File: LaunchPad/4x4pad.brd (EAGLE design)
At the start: 127 x 102.5 mm, 17 parts

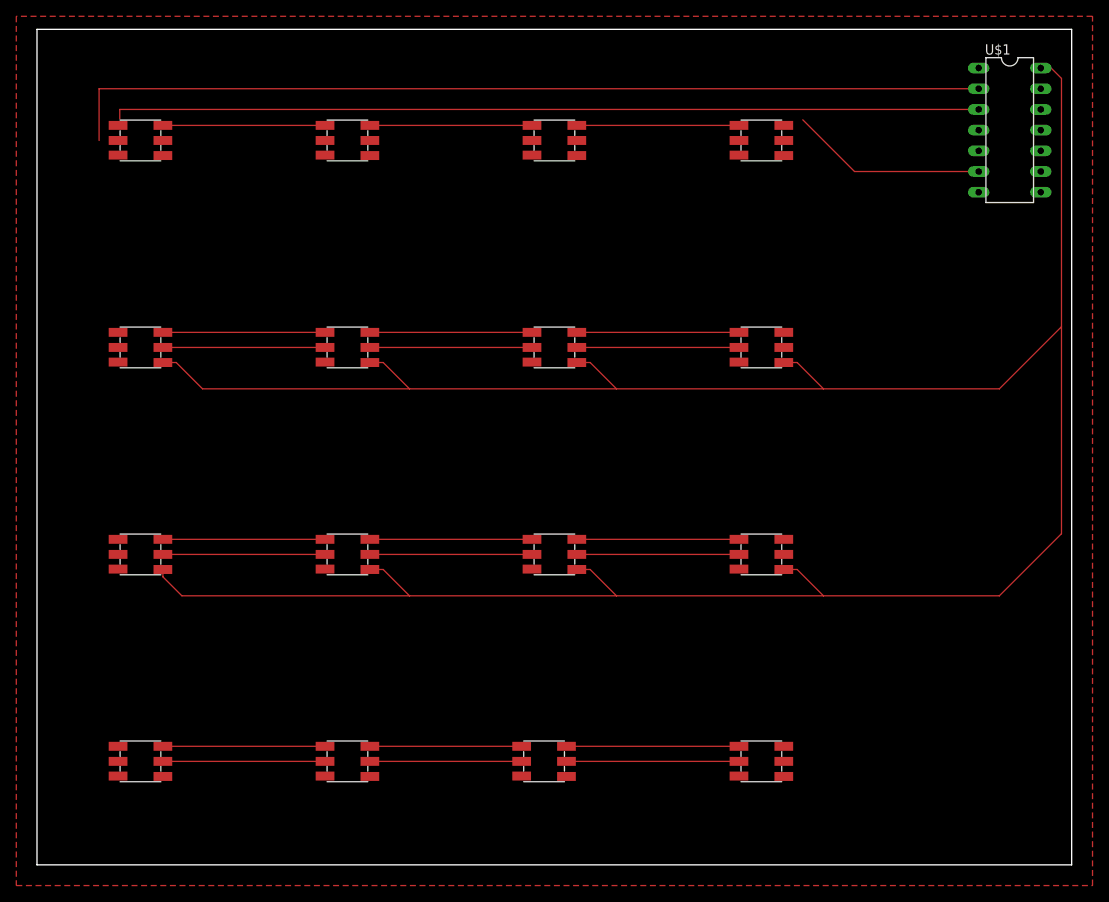
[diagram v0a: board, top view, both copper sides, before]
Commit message: Restarted 4x4 board, still need vertical button jumpoers, button connection
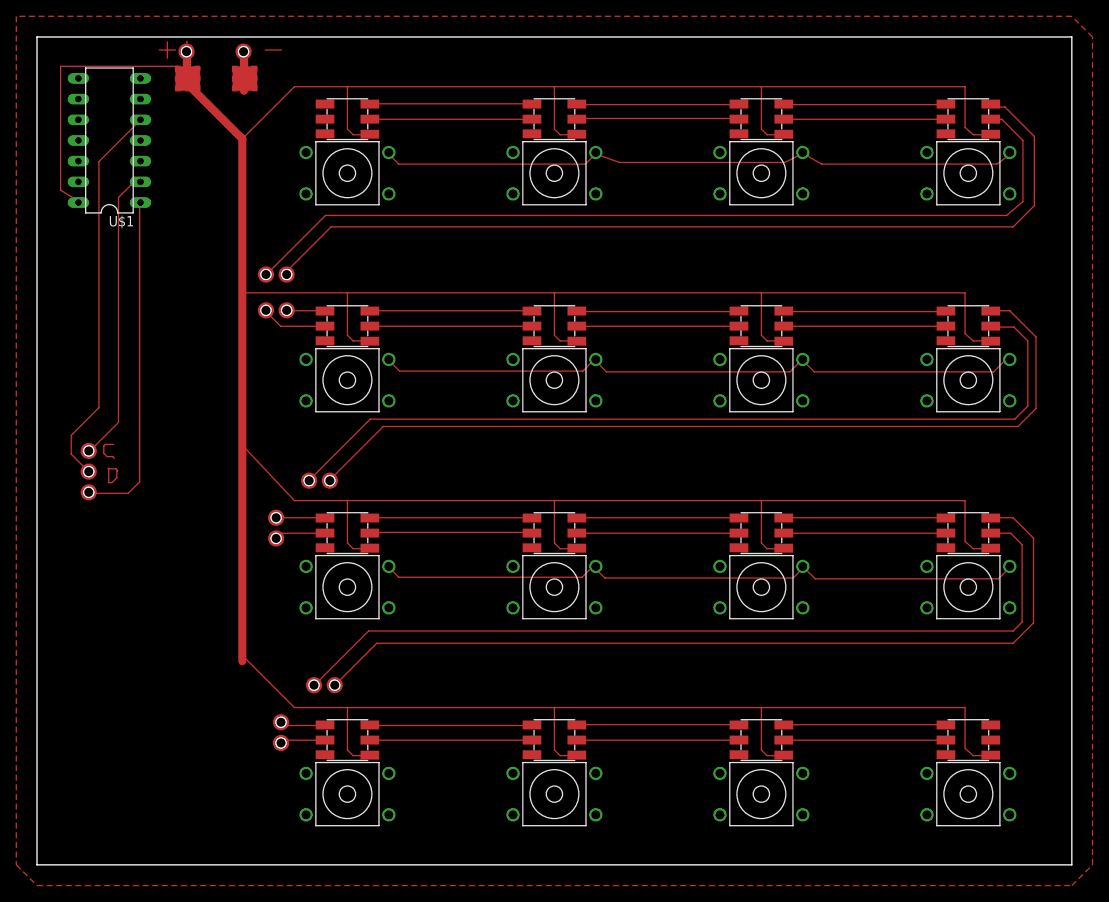
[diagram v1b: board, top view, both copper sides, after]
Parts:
- added U$18, U$19, U$20, U$21, U$22, U$23, U$24, U$25, U$26, U$27, U$28, U$29, U$30, U$31, U$32, U$33: SOFT-TACTILE-PUSHBUTTON, launchpadParts:ADAFRUIT-SOFT-TACTILE-PUSHBUTTON
- moved U$1 110.5 mm to (8.89, 88.9), turned to 90 degrees
- moved U$16 26.8 mm to (88.9, 15.3)
- moved U$12 25.5 mm to (88.9, 40.7)
- moved U$4 25.5 mm to (88.9, 91.5)
- moved U$8 25.5 mm to (88.9, 66.1)
- moved U$10 25.5 mm to (38.1, 40.7)
- moved U$14 25.5 mm to (38.1, 15.3)
- moved U$2 25.5 mm to (38.1, 91.5)
- moved U$6 25.5 mm to (38.1, 66.1)
- moved U$11 25.5 mm to (63.5, 40.7)
- moved U$15 25.5 mm to (63.5, 15.3)
- moved U$3 25.5 mm to (63.5, 91.5)
- moved U$7 25.5 mm to (63.5, 66.1)
- moved U$13 25.5 mm to (114.3, 40.7)
- moved U$17 25.5 mm to (114.3, 15.3)
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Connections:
- net +5V renamed N$36
- net GND renamed N$37
- new net COL1: U$18.P$1, U$18.P$2, U$30.P$1, U$30.P$2
- new net COL2: U$19.P$1, U$19.P$2, U$31.P$1, U$31.P$2
- new net COL3: U$20.P$1, U$20.P$2, U$32.P$1, U$32.P$2
- new net COL4: U$21.P$1, U$21.P$2, U$33.P$1, U$33.P$2
- new net ROW1: U$18.P$3, U$18.P$4, U$19.P$3, U$19.P$4, U$20.P$3, U$20.P$4, U$21.P$3, U$21.P$4
- new net ROW2: U$22.P$3, U$22.P$4, U$23.P$3, U$23.P$4, U$24.P$3, U$24.P$4, U$25.P$3, U$25.P$4
- new net ROW3: U$26.P$3, U$26.P$4, U$27.P$3, U$27.P$4, U$28.P$3, U$28.P$4, U$29.P$3, U$29.P$4
- new net ROW4: U$30.P$3, U$30.P$4, U$31.P$3, U$31.P$4, U$32.P$3, U$32.P$4, U$33.P$3, U$33.P$4
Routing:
- net N$36: track 326.3 -> 0.00 mm
- net N$31: track 0.00 -> 173.2 mm
- net CLK3.3: track 114.3 -> 0.00 mm
- net N$94: track 0.00 -> 110.6 mm
- net N$93: track 0.00 -> 108.5 mm
- net CLK5: track 106.6 -> 0.00 mm
- net N$102: track 0.00 -> 106.1 mm
- net N$105: track 0.00 -> 105.6 mm
- net N$103: track 0.00 -> 104.9 mm
- net N$104: track 0.00 -> 104.0 mm
- net N$40: track 0.00 -> 100.1 mm
- net N$86: track 0.00 -> 99.8 mm
- net N$56: track 0.00 -> 97.1 mm
- net N$97: track 0.00 -> 79.2 mm
- net N$96: track 0.00 -> 52.8 mm
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- added copper zone on layer 1, net GND
- added copper zone on layer 1, net VCC
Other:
- board size 127 x 102.5 mm -> 127 x 101.6 mm

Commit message: idk what I did
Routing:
- net N$118: track 0.00 -> 5.94 mm
- net N$116: track 0.00 -> 5.94 mm
- net N$114: track 0.00 -> 5.94 mm
- net N$113: track 0.00 -> 5.94 mm
- net N$120: track 0.00 -> 5.94 mm
- net N$115: track 0.00 -> 5.94 mm
- net N$112: track 0.00 -> 5.94 mm
- net N$119: track 0.00 -> 5.94 mm
- net N$117: track 0.00 -> 5.94 mm
- net N$92: track 0.00 -> 4.90 mm
- net N$110: track 0.00 -> 4.90 mm
- net N$109: track 0.00 -> 4.90 mm
- net N$107: track 0.00 -> 4.90 mm
- net N$111: track 0.00 -> 4.90 mm
- net N$108: track 0.00 -> 4.90 mm
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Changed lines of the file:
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@@
 <hole x="36.54" y="22.05" drill="1.27"/>
 <circle x="36.54" y="22.05" radius="0.803215625" width="0.381" layer="1"/>
+<hole x="104.3" y="82.35" drill="1.27"/>
+<circle x="104.3" y="82.35" radius="0.803215625" width="0.381" layer="1"/>
+<hole x="78.9" y="82.25" drill="1.27"/>
+<circle x="78.9" y="82.25" radius="0.803215625" width="0.381" layer="1"/>
+<hole x="53.5" y="82.25" drill="1.27"/>
+<circle x="53.5" y="82.25" radius="0.803215625" width="0.381" layer="1"/>
+<hole x="104.4" y="56.85" drill="1.27"/>
+<circle x="104.4" y="56.85" radius="0.803215625" width="0.381" layer="1"/>
+<hole x="78.9" y="56.85" drill="1.27"/>
+<circle x="78.9" y="56.85" radius="0.803215625" width="0.381" layer="1"/>
+<hole x="53.5" y="56.85" drill="1.27"/>
+<circle x="53.5" y="56.85" radius="0.803215625" width="0.381" layer="1"/>
+<hole x="53.5" y="31.45" drill="1.27"/>
+<circle x="53.5" y="31.45" radius="0.803215625" width="0.381" layer="1"/>
+<hole x="78.9" y="31.45" drill="1.27"/>
+<circle x="78.9" y="31.45" radius="0.803215625" width="0.381" layer="1"/>
+<hole x="104.3" y="31.45" drill="1.27"/>
+<circle x="104.3" y="31.45" radius="0.803215625" width="0.381" layer="1"/>
+<hole x="53.5" y="64.55" drill="1.27"/>
+<circle x="53.5" y="64.55" radius="0.803215625" width="0.381" layer="1"/>
+<hole x="79" y="64.55" drill="1.27"/>
+<circle x="79" y="64.55" radius="0.803215625" width="0.381" layer="1"/>
+<hole x="104.3" y="64.55" drill="1.27"/>
+<circle x="104.3" y="64.55" radius="0.803215625" width="0.381" layer="1"/>
+<hole x="53.6" y="39.15" drill="1.27"/>
+<circle x="53.6" y="39.15" radius="0.803215625" width="0.381" layer="1"/>
+<hole x="79" y="39.15" drill="1.27"/>
+<circle x="79" y="39.15" radius="0.803215625" width="0.381" layer="1"/>
+<hole x="104.4" y="39.25" drill="1.27"/>
+<circle x="104.4" y="39.25" radius="0.803215625" width="0.381" layer="1"/>
+<hole x="104.3" y="13.75" drill="1.27"/>
+<circle x="104.3" y="13.75" radius="0.803215625" width="0.381" layer="1"/>
+<hole x="78.9" y="13.75" drill="1.27"/>
+<circle x="78.9" y="13.75" radius="0.803215625" width="0.381" layer="1"/>
+<hole x="53.5" y="13.75" drill="1.27"/>
+<circle x="53.5" y="13.75" radius="0.803215625" width="0.381" layer="1"/>
 </plain>
 <attributes>
@@
 <wire x1="111.6" y1="91.5" x2="111.6" y2="91.4" width="0.1524" layer="1"/>
 </signal>
-<signal name="N$49">
-<wire x1="109.4" y1="31.3" x2="109.2" y2="31.3" width="0.1524" layer="1"/>
-</signal>
-<signal name="N$50">
-<wire x1="109.5" y1="57.1" x2="109.4" y2="57.1" width="0.1524" layer="1"/>
-</signal>
 <signal name="N$51">
 <wire x1="119.6" y1="87.3" x2="117.8" y2="86" width="0.1524" layer="1"/>
@@
 <wire x1="29.9" y1="66.1" x2="28.1" y2="67.9" width="0.125" layer="1"/>
 </signal>
+<signal name="N$92">
+<wire x1="104.3" y1="82.4" x2="109.2" y2="82.4" width="0.1524" layer="1"/>
+</signal>
+<signal name="N$106">
+<wire x1="78.9" y1="82.3" x2="83.8" y2="82.3" width="0.1524" layer="1"/>
+</signal>
+<signal name="N$107">
+<wire x1="53.5" y1="82.3" x2="58.4" y2="82.3" width="0.1524" layer="1"/>
+</signal>
+<signal name="N$50">
+<wire x1="104.4" y1="56.9" x2="109.3" y2="56.9" width="0.1524" layer="1"/>
+</signal>
+<signal name="N$108">
+<wire x1="78.9" y1="56.9" x2="83.8" y2="56.9" width="0.1524" layer="1"/>
+</signal>
+<signal name="N$109">
+<wire x1="53.5" y1="56.9" x2="58.4" y2="56.9" width="0.1524" layer="1"/>
+</signal>
+<signal name="N$110">
+<wire x1="53.5" y1="31.5" x2="58.4" y2="31.5" width="0.1524" layer="1"/>
+</signal>
+<signal name="N$111">
+<wire x1="78.9" y1="31.5" x2="83.8" y2="31.5" width="0.1524" layer="1"/>
+</signal>
+<signal name="N$49">
+<wire x1="104.3" y1="31.5" x2="109.2" y2="31.5" width="0.1524" layer="1"/>
+</signal>
+<signal name="N$112">
+<wire x1="58.4" y1="62" x2="56" y2="62" width="0.1524" layer="1"/>
+<wire x1="56" y1="62" x2="53.5" y2="64.5" width="0.1524" layer="1"/>
+</signal>
+<signal name="N$113">
+<wire x1="83.9" y1="62" x2="81.5" y2="62" width="0.1524" layer="1"/>
+<wire x1="81.5" y1="62" x2="79" y2="64.5" width="0.1524" layer="1"/>
+</signal>
+<signal name="N$114">
+<wire x1="109.2" y1="62" x2="106.8" y2="62" width="0.1524" layer="1"/>
+<wire x1="106.8" y1="62" x2="104.3" y2="64.5" width="0.1524" layer="1"/>
+</signal>
+<signal name="N$115">
+<wire x1="58.5" y1="36.6" x2="56.1" y2="36.6" width="0.1524" layer="1"/>
+<wire x1="56.1" y1="36.6" x2="53.6" y2="39.1" width="0.1524" layer="1"/>
+</signal>
+<signal name="N$116">
+<wire x1="83.9" y1="36.6" x2="81.5" y2="36.6" width="0.1524" layer="1"/>
+<wire x1="81.5" y1="36.6" x2="79" y2="39.1" width="0.1524" layer="1"/>
+</signal>
+<signal name="N$117">
+<wire x1="109.3" y1="36.7" x2="106.9" y2="36.7" width="0.1524" layer="1"/>
+<wire x1="106.9" y1="36.7" x2="104.4" y2="39.2" width="0.1524" layer="1"/>
+</signal>
+<signal name="N$118">
+<wire x1="109.2" y1="11.2" x2="106.8" y2="11.2" width="0.1524" layer="1"/>
+<wire x1="106.8" y1="11.2" x2="104.3" y2="13.7" width="0.1524" layer="1"/>
+</signal>
+<signal name="N$119">
+<wire x1="83.8" y1="11.2" x2="81.4" y2="11.2" width="0.1524" layer="1"/>
+<wire x1="81.4" y1="11.2" x2="78.9" y2="13.7" width="0.1524" layer="1"/>
+</signal>
+<signal name="N$120">
+<wire x1="58.4" y1="11.2" x2="56" y2="11.2" width="0.1524" layer="1"/>
+<wire x1="56" y1="11.2" x2="53.5" y2="13.7" width="0.1524" layer="1"/>
+</signal>
 </signals>

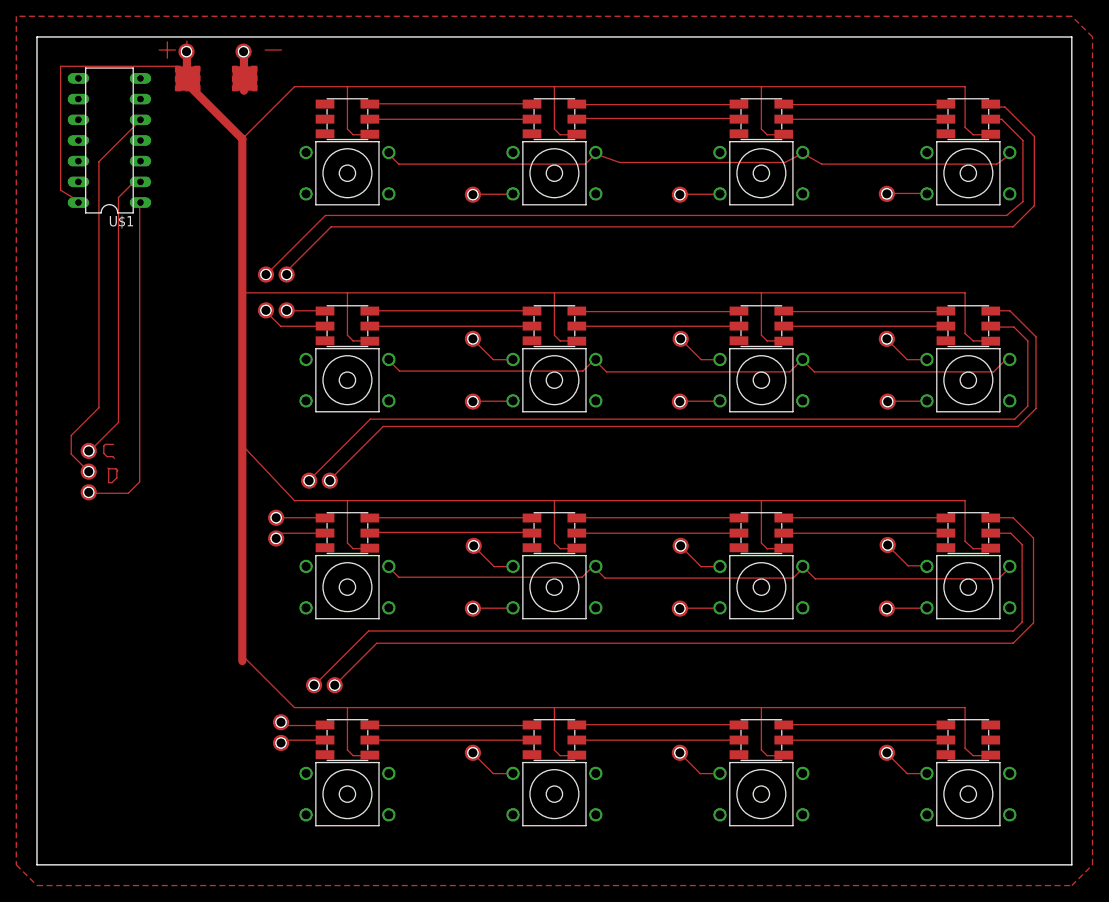
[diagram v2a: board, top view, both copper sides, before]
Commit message: Added jumpers for buttons vertically, added points for ends of button matrix. Added jumpers for led signals
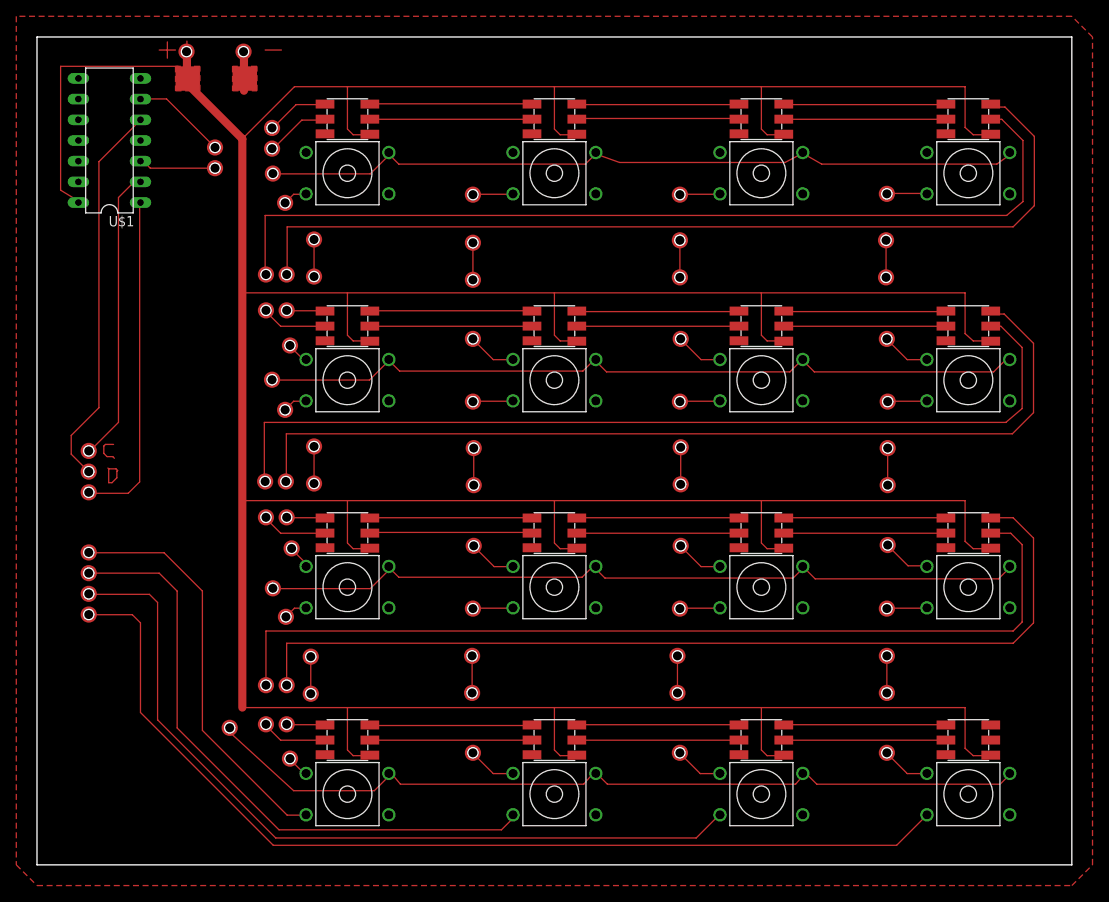
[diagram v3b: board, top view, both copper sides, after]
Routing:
- net N$133: track 0.00 -> 122.8 mm
- net N$63: track 0.14 -> 99.5 mm
- net N$130: track 0.00 -> 79.3 mm
- net N$132: track 0.00 -> 75.8 mm
- net N$131: track 0.00 -> 50.1 mm
- net N$137: track 0.00 -> 23.7 mm
- net N$135: track 0.00 -> 15.3 mm
- net N$134: track 0.00 -> 15.3 mm
- net N$136: track 0.00 -> 15.3 mm
- net N$150: track 0.00 -> 11.7 mm
- net N$104: track 104.0 -> 113.8 mm
- net N$149: track 0.00 -> 9.27 mm
- net N$105: track 105.6 -> 114.5 mm
- net N$103: track 104.9 -> 113.8 mm
- net N$148: track 0.00 -> 7.85 mm
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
